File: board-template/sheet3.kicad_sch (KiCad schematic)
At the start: 0 parts

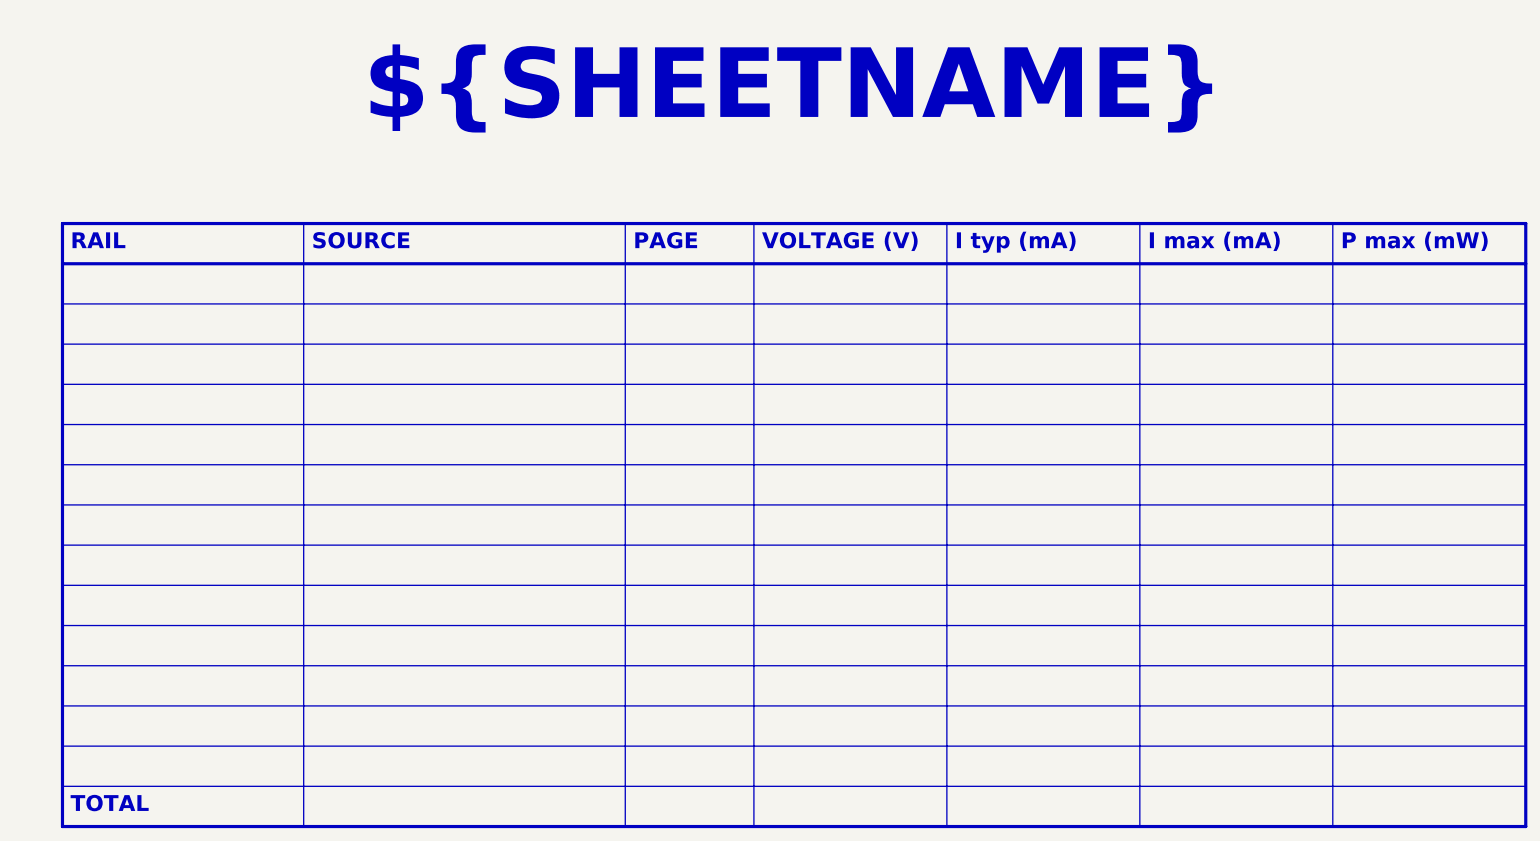
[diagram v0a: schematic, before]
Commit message: template(refact): improve block diagram and power budget
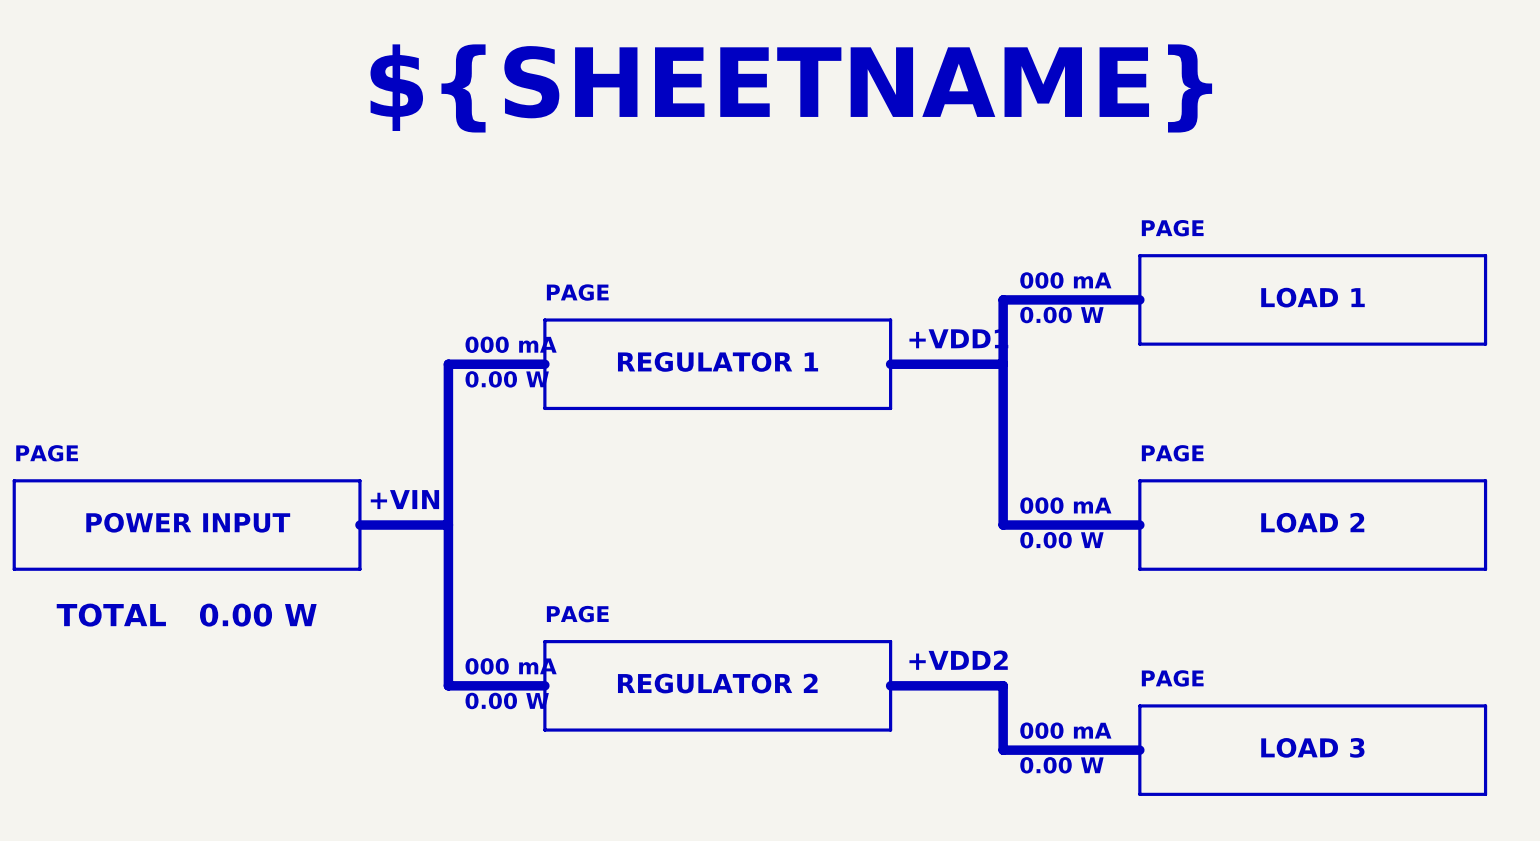
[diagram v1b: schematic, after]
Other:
- note added: "+VDD1"
- note added: "+VDD2"
- note added: "+VIN"
- note added: "0.00 W"
- note added: "000 mA"
- note added: "LOAD 1"
- note added: "LOAD 2"
- note added: "LOAD 3"
- note added: "POWER INPUT"
- note added: "REGULATOR 1"
- note added: "REGULATOR 2"
- note added: "TOTAL 0.00 W"
- note removed: "I max (mA)"
- note removed: "I typ (mA)"
- note removed: "P max (mW)"
- note removed: "RAIL"
- note removed: "SOURCE"
- note removed: "TOTAL"
- note removed: "VOLTAGE (V)"
